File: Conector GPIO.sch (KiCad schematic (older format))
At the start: 4 parts, among them P12 CONN_10X2, P14 SPI

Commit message: resolución fijada en 16 bits y modo configuración fijado
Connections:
- no-connect marks 10 -> 12
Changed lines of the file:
@@
 $Descr A4 11693 8268
 encoding utf-8
-Sheet 4 4
+Sheet 3 4
 Title ""
 Date ""
@@
 NoConn ~ 5250 2650
 NoConn ~ 5200 3600
+NoConn ~ 6600 2150
+NoConn ~ 5250 2250
 $EndSCHEMATC

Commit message: agregado el segundo RDC, leds conectados a +5v, asignados footprints
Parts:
- removed TH8: MF-MSMF030-2, ~, symbol Device:Thermistor
- removed TH9: MF-MSMF110-2, ~, symbol Device:Thermistor
- P12: footprint (none) -> Connector_PinSocket_2.54mm:PinSocket_2x10_P2.54mm_Vertical
- P14: footprint (none) -> Connector_PinSocket_2.54mm:PinSocket_2x03_P2.54mm_Vertical
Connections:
- wire segments 36 -> 35
- no-connect marks 12 -> 11
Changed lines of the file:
@@
 $Descr A4 11693 8268
 encoding utf-8
-Sheet 3 4
+Sheet 2 5
 Title ""
 Date ""
@@
 Wire Wire Line
 	6300 2650 6600 2650
-$Comp
-L Device:Thermistor TH8
-U 1 1 52CA1D91
-P 4350 1750
-F 0 "TH8" V 4450 1800 50  0000 C CNN
-F 1 "MF-MSMF030-2" V 4250 1750 50  0000 C CNN
-F 2 "~" H 4350 1750 60  0000 C CNN
-F 3 "~" H 4350 1750 60  0000 C CNN
-	1    4350 1750
-	0    -1   -1   0
-$EndComp
 Text Label 4800 1750 0    60   ~ 0
 USR_3.3V
@@
 $EndComp
 $Comp
-L Device:Thermistor TH9
-U 1 1 52CA1E88
-P 7500 1750
-F 0 "TH9" V 7600 1800 50  0000 C CNN
-F 1 "MF-MSMF110-2" V 7400 1750 50  0000 C CNN
-F 2 "~" H 7500 1750 60  0000 C CNN
-F 3 "~" H 7500 1750 60  0000 C CNN
-	1    7500 1750
-	0    -1   -1   0
-$EndComp
-$Comp
 L power:GND #PWR0127
 U 1 1 52CA1EC3
@@
 F 0 "P14" H 5850 3800 50  0000 C CNN
 F 1 "SPI" V 5850 3600 40  0000 C CNN
-F 2 "" H 5850 3550 60  0000 C CNN
+F 2 "Connector_PinSocket_2.54mm:PinSocket_2x03_P2.54mm_Vertical" H 5850 3550 60  0001 C CNN
 F 3 "" H 5850 3550 60  0000 C CNN
 	1    5850 3550
@@
 F 0 "P12" H 5900 2750 60  0000 C CNN
 F 1 "CONN_10X2" V 5900 2100 50  0000 C CNN
-F 2 "" H 5900 2200 60  0000 C CNN
+F 2 "Connector_PinSocket_2.54mm:PinSocket_2x10_P2.54mm_Vertical" H 5900 2200 60  0001 C CNN
 F 3 "" H 5900 2200 60  0000 C CNN
 	1    5900 2200
@@
 	8300 1950 8300 1900
 Wire Wire Line
-	4550 1750 5500 1750
-Wire Wire Line
-	6300 1750 7300 1750
-Wire Wire Line
 	7700 1750 7800 1750
 $Comp
@@
 Wire Wire Line
 	6300 1950 8300 1950
-Connection ~ 7700 1750
 Connection ~ 4100 1750
-Wire Wire Line
-	4100 1750 4150 1750
 Wire Wire Line
 	4000 1750 4100 1750
@@
 NoConn ~ 5250 2650
 NoConn ~ 5200 3600
-NoConn ~ 6600 2150
 NoConn ~ 5250 2250
+Wire Wire Line
+	4100 1750 5500 1750
+Wire Wire Line
+	6300 1750 7700 1750
+Connection ~ 7700 1750
 $EndSCHEMATC

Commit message: cambios en el placement
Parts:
- renumbered P12 to P1, P14 to P2
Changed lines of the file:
@@
 USR_3.3V
 $Comp
-L power:+3.3V #PWR0126
+L power:+3.3V #PWR01
 U 1 1 52CA1E6C
 P 4000 1750
-F 0 "#PWR0126" H 4000 1710 30  0001 C CNN
+F 0 "#PWR01" H 4000 1710 30  0001 C CNN
 F 1 "+3.3V" H 4000 1860 30  0000 C CNN
 F 2 "" H 4000 1750 60  0000 C CNN
@@
 $EndComp
 $Comp
-L power:GND #PWR0127
+L power:GND #PWR05
 U 1 1 52CA1EC3
 P 5300 2800
-F 0 "#PWR0127" H 5300 2800 30  0001 C CNN
+F 0 "#PWR05" H 5300 2800 30  0001 C CNN
 F 1 "GND" H 5300 2730 30  0001 C CNN
 F 2 "" H 5300 2800 60  0000 C CNN
@@
 $EndComp
 $Comp
-L power:GND #PWR0128
+L power:GND #PWR06
 U 1 1 52CA1EC9
 P 6550 2800
-F 0 "#PWR0128" H 6550 2800 30  0001 C CNN
+F 0 "#PWR06" H 6550 2800 30  0001 C CNN
 F 1 "GND" H 6550 2730 30  0001 C CNN
 F 2 "" H 6550 2800 60  0000 C CNN
@@
 SPI_CS
 $Comp
-L power:+5V #PWR0129
+L power:+5V #PWR02
 U 1 1 52CA305A
 P 7800 1750
-F 0 "#PWR0129" H 7800 1840 20  0001 C CNN
+F 0 "#PWR02" H 7800 1840 20  0001 C CNN
 F 1 "+5V" H 7800 1840 30  0000 C CNN
 F 2 "" H 7800 1750 60  0000 C CNN
@@
 $EndComp
 $Comp
-L conn_3x2:CONN_3X2 P14
+L conn_3x2:CONN_3X2 P2
 U 1 1 52CCD42B
 P 5850 3550
-F 0 "P14" H 5850 3800 50  0000 C CNN
+F 0 "P2" H 5850 3800 50  0000 C CNN
 F 1 "SPI" V 5850 3600 40  0000 C CNN
 F 2 "Connector_PinSocket_2.54mm:PinSocket_2x03_P2.54mm_Vertical" H 5850 3550 60  0001 C CNN
@@
 	5000 3500 5450 3500
 $Comp
-L power:GND #PWR0132
+L power:GND #PWR07
 U 1 1 52CCD441
 P 6300 3650
-F 0 "#PWR0132" H 6300 3650 30  0001 C CNN
+F 0 "#PWR07" H 6300 3650 30  0001 C CNN
 F 1 "GND" H 6300 3580 30  0001 C CNN
 F 2 "" H 6300 3650 60  0000 C CNN
@@
 Conectores de expansión LVTTL.\nEn formato de pines, 2.54mm de pitch.
 $Comp
-L conn_10x2:CONN_10X2 P12
+L conn_10x2:CONN_10X2 P1
 U 1 1 5343059D
 P 5900 2200
-F 0 "P12" H 5900 2750 60  0000 C CNN
+F 0 "P1" H 5900 2750 60  0000 C CNN
 F 1 "CONN_10X2" V 5900 2100 50  0000 C CNN
 F 2 "Connector_PinSocket_2.54mm:PinSocket_2x10_P2.54mm_Vertical" H 5900 2200 60  0001 C CNN
@@
 $EndComp
 $Comp
-L power:+24V #PWR0135
+L power:+24V #PWR04
 U 1 1 53430CCE
 P 8300 1900
-F 0 "#PWR0135" H 8300 1850 20  0001 C CNN
+F 0 "#PWR04" H 8300 1850 20  0001 C CNN
 F 1 "+24V" H 8300 2000 30  0000 C CNN
 F 2 "" H 8300 1900 60  0000 C CNN
@@
 $EndComp
 $Comp
-L power:+24V #PWR0136
+L power:+24V #PWR03
 U 1 1 53430CDB
 P 3550 1850
-F 0 "#PWR0136" H 3550 1800 20  0001 C CNN
+F 0 "#PWR03" H 3550 1800 20  0001 C CNN
 F 1 "+24V" H 3550 1950 30  0000 C CNN
 F 2 "" H 3550 1850 60  0000 C CNN
@@
 	7700 1750 7800 1750
 $Comp
-L power:PWR_FLAG #FLG0102
+L power:PWR_FLAG #FLG01
 U 1 1 5EF2C0E5
 P 4100 1750
-F 0 "#FLG0102" H 4100 1825 50  0001 C CNN
+F 0 "#FLG01" H 4100 1825 50  0001 C CNN
 F 1 "PWR_FLAG" H 4100 1923 50  0000 C CNN
 F 2 "" H 4100 1750 50  0001 C CNN
@@
 $EndComp
 $Comp
-L power:PWR_FLAG #FLG0103
+L power:PWR_FLAG #FLG02
 U 1 1 5EF2C65F
 P 7700 1750
-F 0 "#FLG0103" H 7700 1825 50  0001 C CNN
+F 0 "#FLG02" H 7700 1825 50  0001 C CNN
 F 1 "PWR_FLAG" H 7700 1923 50  0000 C CNN
 F 2 "" H 7700 1750 50  0001 C CNN
@@
 $EndComp
 $Comp
-L power:PWR_FLAG #FLG0104
+L power:PWR_FLAG #FLG03
 U 1 1 5EF2C8AE
 P 3650 1950
-F 0 "#FLG0104" H 3650 2025 50  0001 C CNN
+F 0 "#FLG03" H 3650 2025 50  0001 C CNN
 F 1 "PWR_FLAG" H 3650 2123 50  0000 C CNN
 F 2 "" H 3650 1950 50  0001 C CNN
@@
 	4000 1750 4100 1750
 $Comp
-L power:PWR_FLAG #FLG0101
+L power:PWR_FLAG #FLG04
 U 1 1 5EF38D95
 P 6600 2800
-F 0 "#FLG0101" H 6600 2875 50  0001 C CNN
+F 0 "#FLG04" H 6600 2875 50  0001 C CNN
 F 1 "PWR_FLAG" H 6600 2973 50  0000 C CNN
 F 2 "" H 6600 2800 50  0001 C CNN

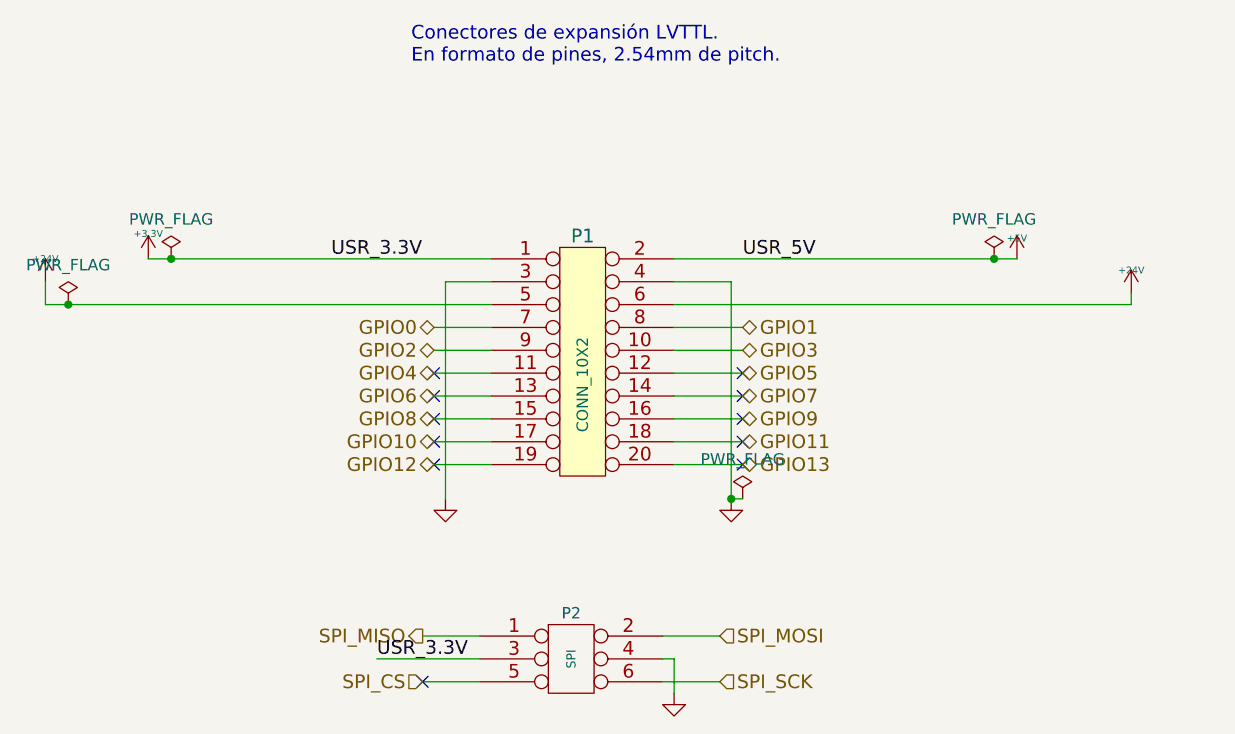
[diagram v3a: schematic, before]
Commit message: routeado completo, quedan 32 vias
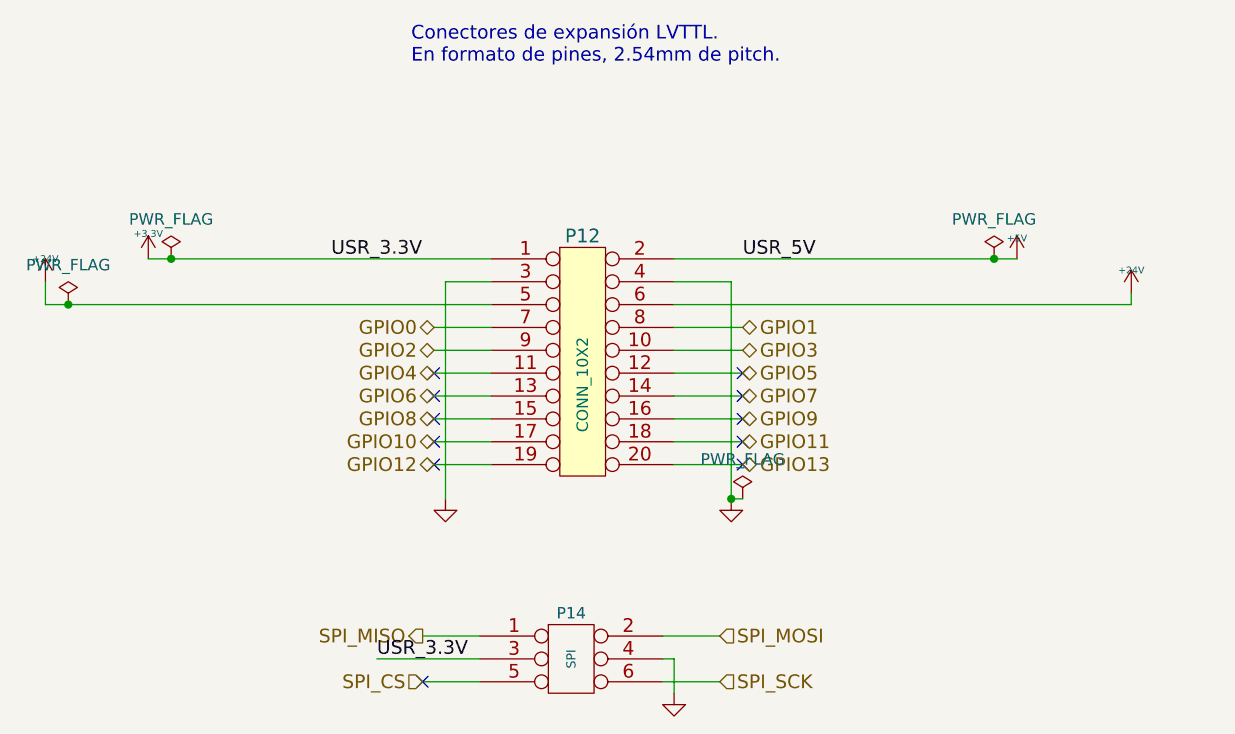
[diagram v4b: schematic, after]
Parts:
- renumbered P1 to P12, P2 to P14
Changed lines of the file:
@@
 $EndComp
 $Comp
-L conn_3x2:CONN_3X2 P2
+L conn_3x2:CONN_3X2 P14
 U 1 1 52CCD42B
 P 5850 3550
-F 0 "P2" H 5850 3800 50  0000 C CNN
+F 0 "P14" H 5850 3800 50  0000 C CNN
 F 1 "SPI" V 5850 3600 40  0000 C CNN
 F 2 "Connector_PinSocket_2.54mm:PinSocket_2x03_P2.54mm_Vertical" H 5850 3550 60  0001 C CNN
@@
 Conectores de expansión LVTTL.\nEn formato de pines, 2.54mm de pitch.
 $Comp
-L conn_10x2:CONN_10X2 P1
+L conn_10x2:CONN_10X2 P12
 U 1 1 5343059D
 P 5900 2200
-F 0 "P1" H 5900 2750 60  0000 C CNN
+F 0 "P12" H 5900 2750 60  0000 C CNN
 F 1 "CONN_10X2" V 5900 2100 50  0000 C CNN
 F 2 "Connector_PinSocket_2.54mm:PinSocket_2x10_P2.54mm_Vertical" H 5900 2200 60  0001 C CNN

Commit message: cambiados conectores, agregado conversor 3,3->TTL drivers
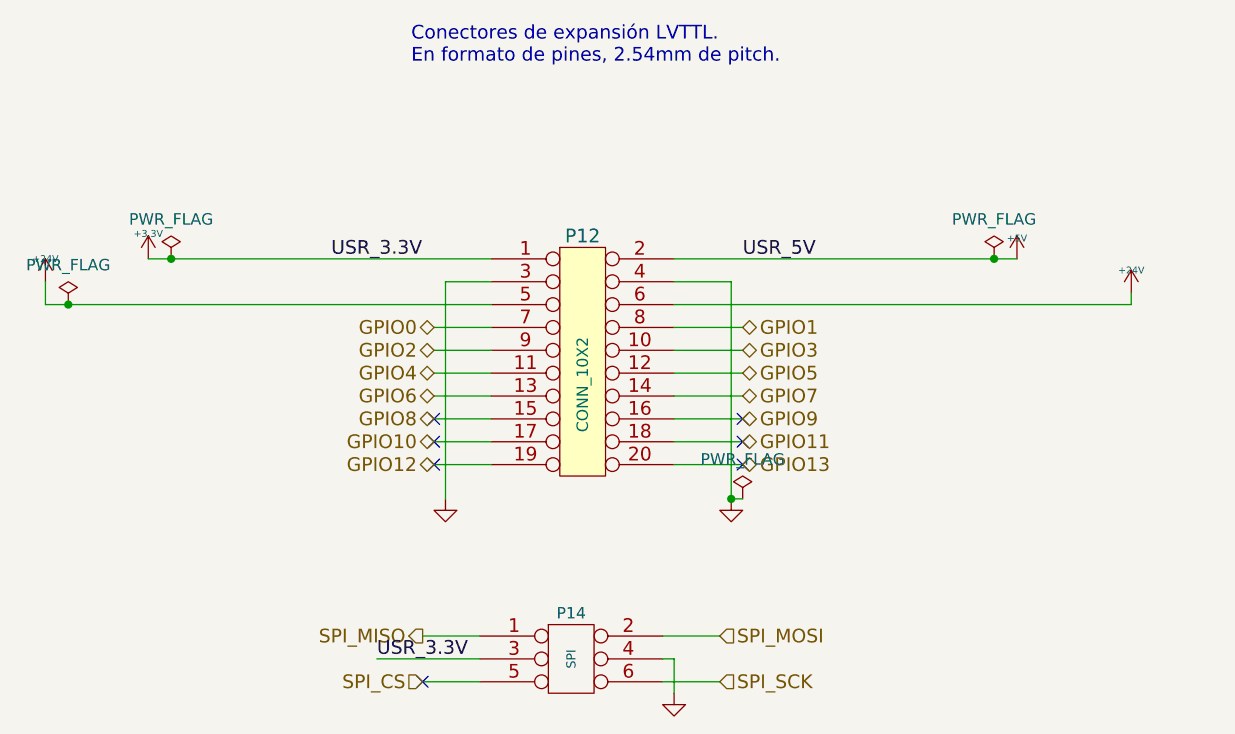
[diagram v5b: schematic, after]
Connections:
- no-connect marks 11 -> 7
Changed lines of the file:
@@
 $Descr A4 11693 8268
 encoding utf-8
-Sheet 2 5
+Sheet 2 6
 Title ""
 Date ""
@@
 Connection ~ 6550 2800
 NoConn ~ 6600 2450
-NoConn ~ 6600 2350
 NoConn ~ 6600 2550
 NoConn ~ 6600 2650
-NoConn ~ 6600 2250
-NoConn ~ 5250 2350
 NoConn ~ 5250 2450
 NoConn ~ 5250 2550
 NoConn ~ 5250 2650
 NoConn ~ 5200 3600
-NoConn ~ 5250 2250
 Wire Wire Line
 	4100 1750 5500 1750

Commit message: eliminado regulador 12v, alimentar CIAA con 12v directamente
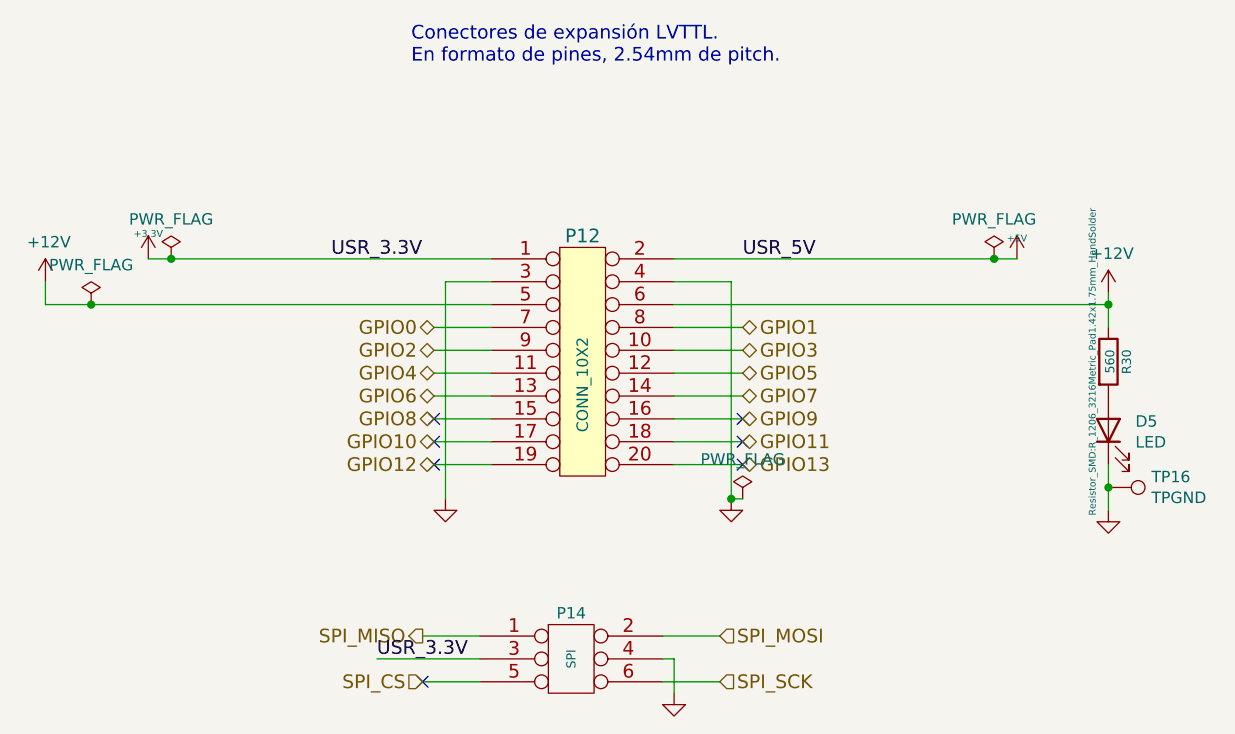
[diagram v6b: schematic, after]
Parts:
- added D5: LED, LED_SMD:LED_1206_3216Metric_Pad1.42x1.75mm_HandSolder, symbol Device:LED
- added R30: 560, Resistor_SMD:R_1206_3216Metric_Pad1.42x1.75mm_HandSolder, symbol Device:R
- added TP16: TPGND, TestPoint:TestPoint_THTPad_1.0x1.0mm_Drill0.5mm, symbol Connector:TestPoint
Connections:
- net GND: now also D5.1 (K), TP16.1
- net +24V renamed +12V
- net +12V: now also R30.1
- new net: D5.2 (A), R30.2
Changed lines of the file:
@@
 $Descr A4 11693 8268
 encoding utf-8
-Sheet 2 6
+Sheet 2 5
 Title ""
 Date ""
@@
 	1    0    0    -1
 $EndComp
-$Comp
-L power:+24V #PWR04
-U 1 1 53430CCE
-P 8300 1900
-F 0 "#PWR04" H 8300 1850 20  0001 C CNN
-F 1 "+24V" H 8300 2000 30  0000 C CNN
-F 2 "" H 8300 1900 60  0000 C CNN
-F 3 "" H 8300 1900 60  0000 C CNN
-	1    8300 1900
-	1    0    0    -1
-$EndComp
-$Comp
-L power:+24V #PWR03
-U 1 1 53430CDB
-P 3550 1850
-F 0 "#PWR03" H 3550 1800 20  0001 C CNN
-F 1 "+24V" H 3550 1950 30  0000 C CNN
-F 2 "" H 3550 1850 60  0000 C CNN
-F 3 "" H 3550 1850 60  0000 C CNN
-	1    3550 1850
-	1    0    0    -1
-$EndComp
-Wire Wire Line
-	5500 1950 3650 1950
 Wire Wire Line
 	3550 1950 3550 1850
-Wire Wire Line
-	8300 1950 8300 1900
 Wire Wire Line
 	7700 1750 7800 1750
@@
 L power:PWR_FLAG #FLG03
 U 1 1 5EF2C8AE
-P 3650 1950
-F 0 "#FLG03" H 3650 2025 50  0001 C CNN
-F 1 "PWR_FLAG" H 3650 2123 50  0000 C CNN
-F 2 "" H 3650 1950 50  0001 C CNN
-F 3 "~" H 3650 1950 50  0001 C CNN
-	1    3650 1950
-	1    0    0    -1
-$EndComp
-Connection ~ 3650 1950
-Wire Wire Line
-	3650 1950 3550 1950
-Wire Wire Line
-	6300 1950 8300 1950
+P 3750 1950
+F 0 "#FLG03" H 3750 2025 50  0001 C CNN
+F 1 "PWR_FLAG" H 3750 2123 50  0000 C CNN
+F 2 "" H 3750 1950 50  0001 C CNN
+F 3 "~" H 3750 1950 50  0001 C CNN
+	1    3750 1950
+	1    0    0    -1
+$EndComp
 Connection ~ 4100 1750
 Wire Wire Line
@@
 	6300 1750 7700 1750
 Connection ~ 7700 1750
+$Comp
+L power:+12V #PWR?
+U 1 1 5F1004FD
+P 8200 1900
+AR Path="/5F1004FD" Ref="#PWR?"  Part="1"
+AR Path="/5EF34214/5F1004FD" Ref="#PWR?"  Part="1"
+AR Path="/5EF2A268/5F1004FD" Ref="#PWR0101"  Part="1"
+F 0 "#PWR0101" H 8200 1750 50  0001 C CNN
+F 1 "+12V" H 8215 2073 50  0000 C CNN
+F 2 "" H 8200 1900 50  0001 C CNN
+F 3 "" H 8200 1900 50  0001 C CNN
+	1    8200 1900
+	1    0    0    -1
+$EndComp
+$Comp
+L Device:R R?
+U 1 1 5F10050A
+P 8200 2200
+AR Path="/5F10050A" Ref="R?"  Part="1"
+AR Path="/5EF45E27/5F10050A" Ref="R?"  Part="1"
+AR Path="/5F077C82/5F10050A" Ref="R?"  Part="1"
+AR Path="/5EF34214/5F10050A" Ref="R?"  Part="1"
+AR Path="/5EF2A268/5F10050A" Ref="R30"  Part="1"
+F 0 "R30" V 8280 2200 40  0000 C CNN
+F 1 "560" V 8207 2201 40  0000 C CNN
+F 2 "Resistor_SMD:R_1206_3216Metric_Pad1.42x1.75mm_HandSolder" V 8130 2200 30  0000 C CNN
+F 3 "~" H 8200 2200 30  0000 C CNN
+	1    8200 2200
+	1    0    0    -1
+$EndComp
+$Comp
+L Device:LED D?
+U 1 1 5F100510
+P 8200 2500
+AR Path="/5F100510" Ref="D?"  Part="1"
+AR Path="/5EF45E27/5F100510" Ref="D?"  Part="1"
+AR Path="/5F077C82/5F100510" Ref="D?"  Part="1"
+AR Path="/5EF34214/5F100510" Ref="D?"  Part="1"
+AR Path="/5EF2A268/5F100510" Ref="D5"  Part="1"
+F 0 "D5" V 8239 2382 50  0000 R CNN
+F 1 "LED" V 8148 2382 50  0000 R CNN
+F 2 "LED_SMD:LED_1206_3216Metric_Pad1.42x1.75mm_HandSolder" H 8200 2500 50  0001 C CNN
+F 3 "~" H 8200 2500 50  0001 C CNN
+	1    8200 2500
+	0    -1   -1   0
+$EndComp
+$Comp
+L power:GND #PWR?
+U 1 1 5F100516
+P 8200 2850
+AR Path="/5F100516" Ref="#PWR?"  Part="1"
+AR Path="/5EF34214/5F100516" Ref="#PWR?"  Part="1"
+AR Path="/5EF2A268/5F100516" Ref="#PWR0102"  Part="1"
+F 0 "#PWR0102" H 8200 2850 30  0001 C CNN
+F 1 "GND" H 8200 2780 30  0001 C CNN
+F 2 "" H 8200 2850 60  0000 C CNN
+F 3 "" H 8200 2850 60  0000 C CNN
+	1    8200 2850
+	1    0    0    -1
+$EndComp
+$Comp
+L Connector:TestPoint TP?
+U 1 1 5F10051C
+P 8200 2750
+AR Path="/5EF34214/5F10051C" Ref="TP?"  Part="1"
+AR Path="/5EF2A268/5F10051C" Ref="TP16"  Part="1"
+F 0 "TP16" V 8154 2938 50  0000 L CNN
+F 1 "TPGND" V 8245 2938 50  0000 L CNN
+F 2 "TestPoint:TestPoint_THTPad_1.0x1.0mm_Drill0.5mm" H 8400 2750 50  0001 C CNN
+F 3 "~" H 8400 2750 50  0001 C CNN
+	1    8200 2750
+	0    1    1    0
+$EndComp
+Wire Wire Line
+	8200 2650 8200 2750
+Connection ~ 8200 2750
+Wire Wire Line
+	8200 2750 8200 2850
+Wire Wire Line
+	8200 1900 8200 1950
+Wire Wire Line
+	6300 1950 8200 1950
+Connection ~ 8200 1950
+Wire Wire Line
+	8200 1950 8200 2050
+Connection ~ 3750 1950
+Wire Wire Line
+	3750 1950 5500 1950
+Wire Wire Line
+	3550 1950 3750 1950
+$Comp
+L power:+12V #PWR?
+U 1 1 5F1138EB
+P 3550 1850
+AR Path="/5F1138EB" Ref="#PWR?"  Part="1"
+AR Path="/5EF34214/5F1138EB" Ref="#PWR?"  Part="1"
+AR Path="/5EF2A268/5F1138EB" Ref="#PWR0103"  Part="1"
+F 0 "#PWR0103" H 3550 1700 50  0001 C CNN
+F 1 "+12V" H 3565 2023 50  0000 C CNN
+F 2 "" H 3550 1850 50  0001 C CNN
+F 3 "" H 3550 1850 50  0001 C CNN
+	1    3550 1850
+	1    0    0    -1
+$EndComp
 $EndSCHEMATC

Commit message: cambiados capacitores electroliticos por tantalio (unpolarized). Agrandado footprint test pads, generado BOM, 35 vias
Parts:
- TP16: footprint TestPoint:TestPoint_THTPad_1.0x1.0mm_Drill0.5mm -> TestPoint:TestPoint_THTPad_1.5x1.5mm_Drill0.7mm
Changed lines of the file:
@@
 F 0 "TP16" V 8154 2938 50  0000 L CNN
 F 1 "TPGND" V 8245 2938 50  0000 L CNN
-F 2 "TestPoint:TestPoint_THTPad_1.0x1.0mm_Drill0.5mm" H 8400 2750 50  0001 C CNN
+F 2 "TestPoint:TestPoint_THTPad_1.5x1.5mm_Drill0.7mm" H 8400 2750 50  0001 C CNN
 F 3 "~" H 8400 2750 50  0001 C CNN
 	1    8200 2750

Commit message: agrandados pads de test points
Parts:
- TP16: footprint TestPoint:TestPoint_THTPad_1.5x1.5mm_Drill0.7mm -> TestPoint:TestPoint_reducido
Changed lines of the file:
@@
 F 0 "TP16" V 8154 2938 50  0000 L CNN
 F 1 "TPGND" V 8245 2938 50  0000 L CNN
-F 2 "TestPoint:TestPoint_THTPad_1.5x1.5mm_Drill0.7mm" H 8400 2750 50  0001 C CNN
+F 2 "TestPoint:TestPoint_reducido" H 8400 2750 50  0001 C CNN
 F 3 "~" H 8400 2750 50  0001 C CNN
 	1    8200 2750
